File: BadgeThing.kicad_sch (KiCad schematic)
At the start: 63 parts, among them J1 USB_C_Receptacle_USB2.0, J2 Connector_Generic_Conn_01x02, J3 Ext 5V, J4 SWD Header, J6 External 3V3, SW1 BOOTSEL, SW2 ESP RESET, SW3 Left, SW4 Down, SW5 Select, SW6 Up, SW7 Right, U2 W25Q32JVSS, U3 RP2040, U4 NCP1117-3.3_SOT223, U5 ESP-12F, Y1 12.000MHz

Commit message: Continue routing
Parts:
- added C24: 100nF, Capacitor_SMD:C_0402_1005Metric_Pad0.74x0.62mm_HandSolder, symbol Device:C_Small
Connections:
- net +3V3: now also C24.1
- net GND: now also C24.2
- net ESP_RST: now reaches SW2.2, U5.1 (~{RST})
- net ESP13: now reaches U5.7 (GPIO13)
- no-connect marks 38 -> 37
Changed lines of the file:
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@@
   (junction (at 254.635 110.49) (diameter 0) (color 0 0 0 0)
   )
+  (junction (at 213.36 24.13) (diameter 0) (color 0 0 0 0)
+  )
   (junction (at 130.81 35.56) (diameter 0) (color 0 0 0 0)
   )
@@
   (junction (at 128.27 35.56) (diameter 0) (color 0 0 0 0)
   )
+  (junction (at 203.2 19.05) (diameter 0) (color 0 0 0 0)
+  )
   (junction (at 66.675 107.95) (diameter 0) (color 0 0 0 0)
   )
@@
   (no_connect (at 153.67 134.62))
   (no_connect (at 25.4 131.445))
-  (no_connect (at 55.88 131.445))
   (no_connect (at 55.88 126.365))
   (no_connect (at 255.27 137.16))
@@
     (stroke (width 0) (type default))
   )
+  (wire (pts (xy 203.2 24.13) (xy 213.36 24.13))
+    (stroke (width 0) (type default))
+  )
   (polyline (pts (xy 241.935 13.335) (xy 283.845 13.335))
     (stroke (width 0) (type default))
@@
     (stroke (width 0) (type default))
   )
+  (wire (pts (xy 203.2 19.05) (xy 213.36 19.05))
+    (stroke (width 0) (type default))
+  )
   (wire (pts (xy 209.55 137.16) (xy 217.17 137.16))
     (stroke (width 0) (type default))
@@
     (stroke (width 0) (type default))
   )
-  (wire (pts (xy 203.2 24.13) (xy 203.2 24.765))
+  (wire (pts (xy 213.36 24.13) (xy 213.36 24.765))
     (stroke (width 0) (type default))
   )
@@
     (stroke (width 0) (type default))
   )
-  (polyline (pts (xy 165.1 150.495) (xy 263.525 150.495))
+  (polyline (pts (xy 166.37 150.495) (xy 263.525 150.495))
     (stroke (width 0) (type default))
   )
@@
     (stroke (width 0) (type default))
   )
-  (polyline (pts (xy 165.1 119.38) (xy 284.988 119.38))
+  (polyline (pts (xy 166.37 119.38) (xy 284.988 119.38))
     (stroke (width 0) (type default))
   )
@@
     (stroke (width 0) (type default))
   )
-  (polyline (pts (xy 165.1 150.495) (xy 165.1 119.38))
+  (polyline (pts (xy 166.37 150.495) (xy 166.37 119.38))
     (stroke (width 0) (type default))
   )
@@
     (stroke (width 0) (type default))
   )
-  (polyline (pts (xy 76.835 150.495) (xy 165.1 150.495))
+  (polyline (pts (xy 76.835 150.495) (xy 166.37 150.495))
     (stroke (width 0) (type default))
   )
@@
     (effects (font (size 1.27 1.27)) (justify left bottom))
   )
-  (text "RGB LEDs" (at 165.735 121.92 0)
+  (text "RGB LEDs" (at 167.005 121.92 0)
     (effects (font (size 1.27 1.27)) (justify left bottom))
   )
@@
     (effects (font (size 1.27 1.27)) (justify left bottom))
   )
+  (label "ESP_RST" (at 17.145 113.665 0) (fields_autoplaced)
+    (effects (font (size 1.27 1.27)) (justify left bottom))
+  )
   (global_label "SCLK" (shape input) (at 153.67 93.98 0) (fields_autoplaced)
     (effects (font (size 1.27 1.27)) (justify left))
@@
     )
   )
+  (global_label "ESP13" (shape input) (at 55.88 131.445 0) (fields_autoplaced)
+    (effects (font (size 1.27 1.27)) (justify left))
+    (property "Intersheetrefs" "${INTERSHEET_REFS}" (at 64.8333 131.445 0)
+      (effects (font (size 1.27 1.27)) (justify left) hide)
+    )
+  )
   (global_label "ESP0" (shape input) (at 74.93 130.175 270) (fields_autoplaced)
     (effects (font (size 1.27 1.27)) (justify right))
@@
     )
   )
-  (symbol (lib_id "power:GND") (at 203.2 24.765 0) (unit 1)
+  (symbol (lib_id "power:GND") (at 213.36 24.765 0) (unit 1)
     (in_bom yes) (on_board yes) (dnp no) (fields_autoplaced)
-    (property "Reference" "#PWR028" (at 203.2 31.115 0)
+    (property "Reference" "#PWR028" (at 213.36 31.115 0)
       (effects (font (size 1.27 1.27)) hide)
     )
-    (property "Value" "GND" (at 203.2 29.845 0)
+    (property "Value" "GND" (at 213.36 29.845 0)
       (effects (font (size 1.27 1.27)))
     )
-    (property "Footprint" "" (at 203.2 24.765 0)
+    (property "Footprint" "" (at 213.36 24.765 0)
       (effects (font (size 1.27 1.27)) hide)
     )
-    (property "Datasheet" "" (at 203.2 24.765 0)
+    (property "Datasheet" "" (at 213.36 24.765 0)
       (effects (font (size 1.27 1.27)) hide)
     )
@@
   )
   (symbol (lib_id "Device:C_Small") (at 203.2 21.59 0) (unit 1)
-    (in_bom yes) (on_board yes) (dnp no) (fields_autoplaced)
-    (property "Reference" "C22" (at 205.74 20.3262 0)
+    (in_bom yes) (on_board yes) (dnp no)
+    (property "Reference" "C22" (at 205.105 20.32 0)
       (effects (font (size 1.27 1.27)) (justify left))
     )
-    (property "Value" "100nF" (at 205.74 22.8662 0)
+    (property "Value" "100nF" (at 205.105 22.86 0)
       (effects (font (size 1.27 1.27)) (justify left))
     )
@@
         )
       )
+    )
+  )
+  (symbol (lib_id "Device:C_Small") (at 213.36 21.59 0) (unit 1)
+    (in_bom yes) (on_board yes) (dnp no)
+    (property "Reference" "C24" (at 215.265 20.32 0)
+      (effects (font (size 1.27 1.27)) (justify left))
+    )
+    (property "Value" "100nF" (at 215.265 22.86 0)
+      (effects (font (size 1.27 1.27)) (justify left))
+    )
+    (property "Footprint" "Capacitor_SMD:C_0402_1005Metric_Pad0.74x0.62mm_HandSolder" (at 213.36 21.59 0)
+      (effects (font (size 1.27 1.27)) hide)
+    )
+    (property "Datasheet" "~" (at 213.36 21.59 0)
+      (effects (font (size 1.27 1.27)) hide)
+    )
+    (property "LCSC" "C1525" (at 213.36 21.59 0)
+      (effects (font (size 1.27 1.27)) hide)
+    )
+    (pin "1")
+    (pin "2")
+    (instances
+      (project "BadgeThing"
+        (path "/35d5f6bf-e39e-48ab-813a-17587fce37db"
+          (reference "C24") (unit 1)
+        )
+      )
+      (project "PicoLX"
+        (path "/c5e5d8b8-bebd-4318-85a6-adbafb95dd10"
+          (reference "C14") (unit 1)
+        )
+      )
+      (project "Panel"
+        (path "/f55927e3-6490-4e79-9229-dceeb24f0064"
+          (reference "C15") (unit 1)
+        )
+      )

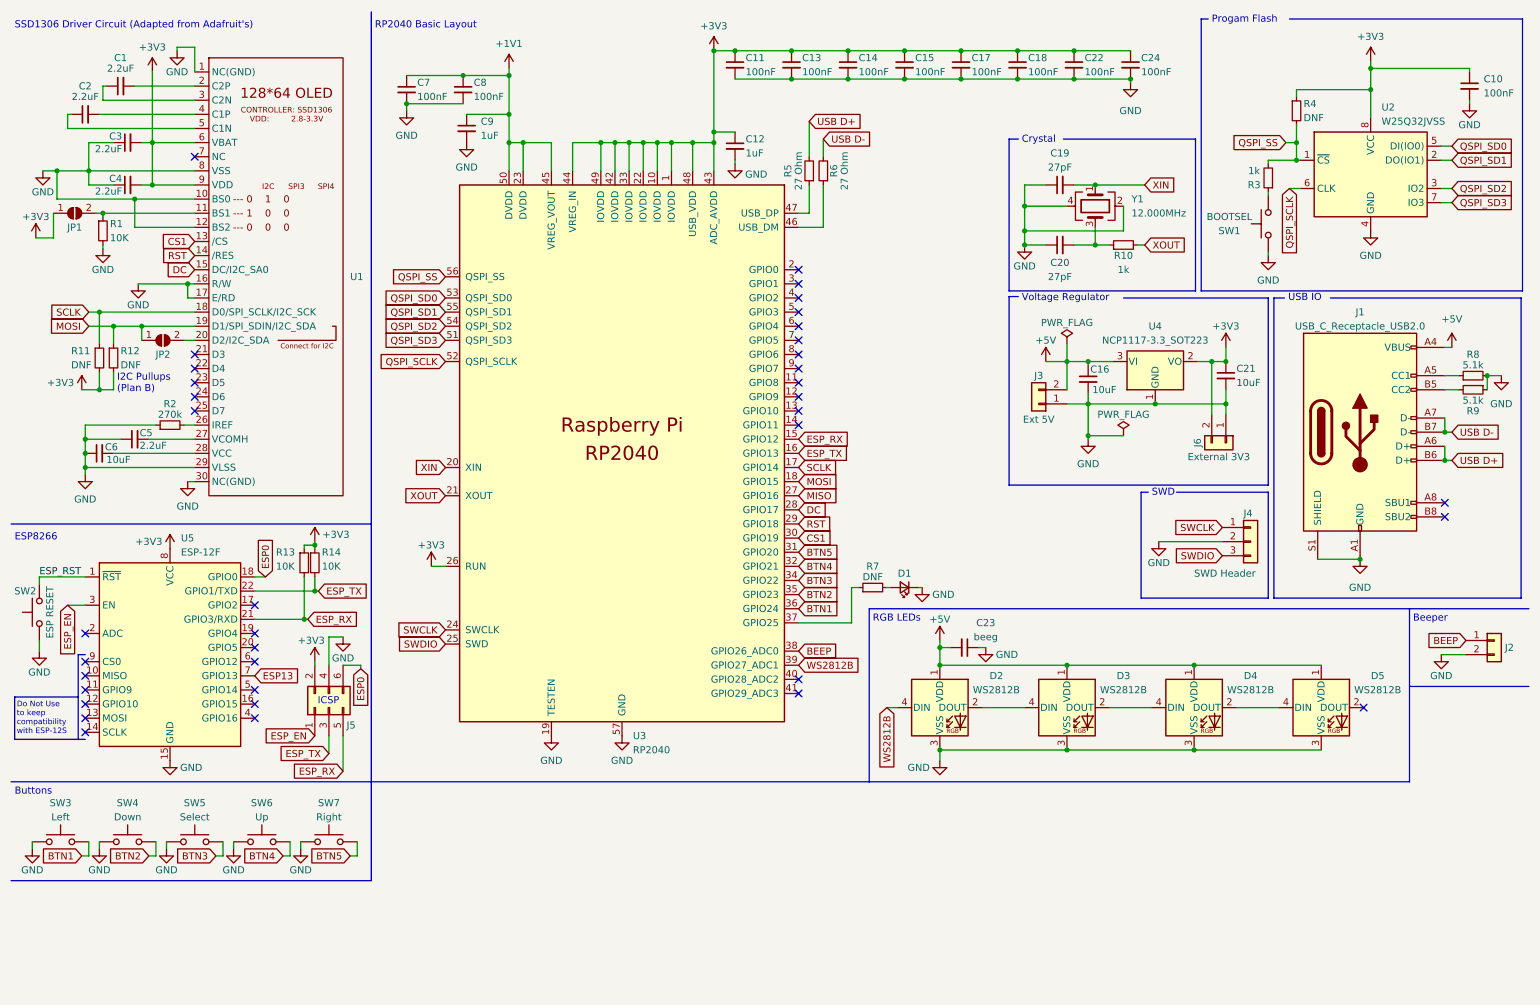
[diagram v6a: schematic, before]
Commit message: huge routing optimizations and extra features
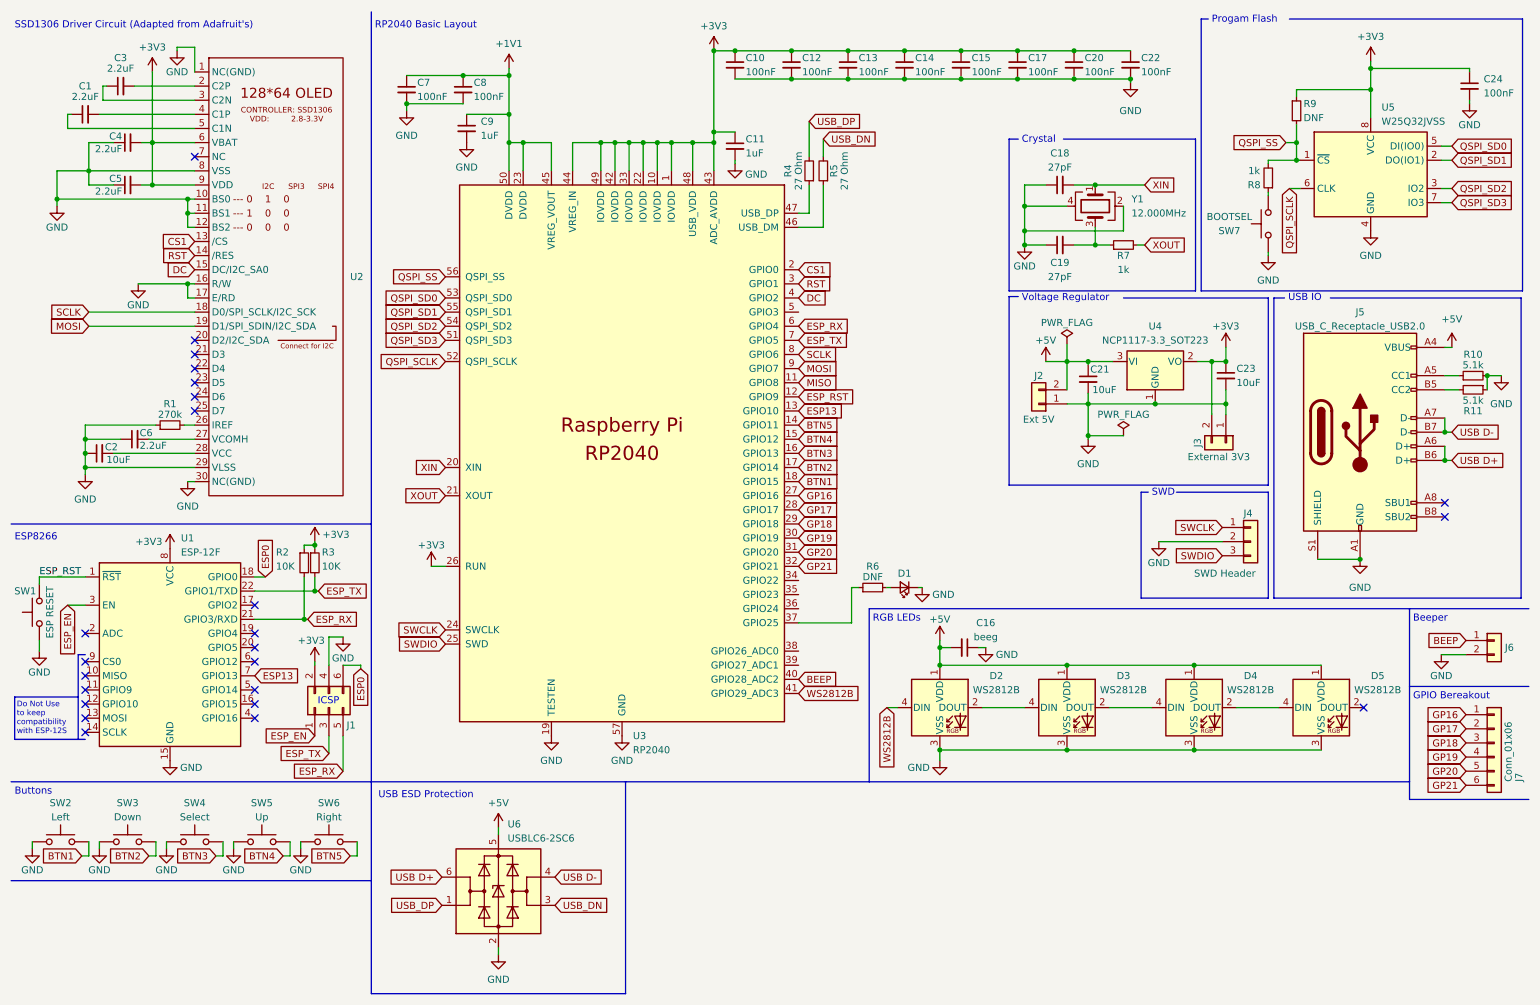
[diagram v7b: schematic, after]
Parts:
- removed JP1, JP2: SolderJumper_2_Open, Jumper:SolderJumper-2_P1.3mm_Open_RoundedPad1.0x1.5mm, symbol Jumper:SolderJumper_2_Open
- removed R1: 10K, Resistor_SMD:R_0402_1005Metric_Pad0.72x0.64mm_HandSolder, symbol Device:R_Small
- removed R11, R12: DNF, Resistor_SMD:R_0402_1005Metric_Pad0.72x0.64mm_HandSolder, symbol Device:R_Small
- added J7: Conn_01x06, Connector_PinHeader_2.00mm:PinHeader_1x06_P2.00mm_Vertical, symbol Connector_Generic:Conn_01x06
- added U6: USBLC6-2SC6, Package_TO_SOT_SMD:SOT-23-6, symbol Power_Protection:USBLC6-2SC6
- C1: renamed from C2; LCSC (none) -> C12530
- C3: renamed from C1; LCSC (none) -> C12530
- C4: renamed from C3; LCSC (none) -> C12530
- C5: renamed from C4; LCSC (none) -> C12530
- C6: renamed from C5; LCSC (none) -> C12530
- renumbered C11 to C10, C12 to C11, C13 to C12, C14 to C13, C15 to C14, C17 to C15, C23 to C16, C18 to C17, C19 to C18, C20 to C19, C6 to C2, C22 to C20, C16 to C21, C24 to C22, C21 to C23, C10 to C24, J5 to J1, J3 to J2, J6 to J3, J1 to J5, J2 to J6, R2 to R1, R8 to R10, R9 to R11, R13 to R2, R14 to R3, R5 to R4, R6 to R5, R7 to R6, R10 to R7, R3 to R8, R4 to R9, SW2 to SW1, SW3 to SW2, SW4 to SW3, SW5 to SW4, SW6 to SW5, SW7 to SW6, SW1 to SW7, U5 to U1, U1 to U2, U2 to U5
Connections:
- net +5V: now also U6.5 (VBUS)
- net BEEP: now also U3.40 (GPIO28_ADC2); no longer U3.38 (GPIO26_ADC0)
- net BTN1: now also U3.18 (GPIO15); no longer U3.36 (GPIO24)
- net BTN2: now also U3.17 (GPIO14); no longer U3.35 (GPIO23)
- net BTN3: now also U3.16 (GPIO13); no longer U3.34 (GPIO22)
- net BTN4: now also U3.15 (GPIO12); no longer U3.32 (GPIO21)
- net BTN5: now also U3.14 (GPIO11); no longer U3.31 (GPIO20)
- net CS1: now also U3.2 (GPIO0); no longer U3.30 (GPIO19)
- net DC: now also U3.4 (GPIO2); no longer U3.28 (GPIO17)
- net ESP13: now also U3.13 (GPIO10)
- net ESP_RST: now also U3.12 (GPIO9)
- net ESP_RX: now also U3.6 (GPIO4); no longer U3.15 (GPIO12)
- net ESP_TX: now also U3.7 (GPIO5); no longer U3.16 (GPIO13)
- net GND: now also U2.11 (BS1), U6.2 (GND)
- net MISO: now also U3.11 (GPIO8); no longer U3.27 (GPIO16)
- net MOSI: now also U3.9 (GPIO7); no longer U3.18 (GPIO15)
- net RST: now also U3.3 (GPIO1); no longer U3.29 (GPIO18)
- net SCLK: now also U3.8 (GPIO6); no longer U3.17 (GPIO14)
- net USB D+: now also U6.6 (I/O1); no longer R4.2
- net USB D-: now also U6.4 (I/O2); no longer R5.2
- net WS2812B: now also U3.41 (GPIO29_ADC3); no longer U3.39 (GPIO27_ADC1)
- new net GP16: J7.1 (Pin_1), U3.27 (GPIO16)
- new net GP17: J7.2 (Pin_2), U3.28 (GPIO17)
- new net GP18: J7.3 (Pin_3), U3.29 (GPIO18)
- new net GP19: J7.4 (Pin_4), U3.30 (GPIO19)
- new net GP20: J7.5 (Pin_5), U3.31 (GPIO20)
- new net GP21: J7.6 (Pin_6), U3.32 (GPIO21)
- new net USB_DN: R5.2, U6.3 (I/O2)
- new net USB_DP: R4.2, U6.1 (I/O1)
- no-connect marks 37 -> 24
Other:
- note added: "GPIO Bereakout"
- note added: "USB ESD Protection"
- note removed: "I2C Pullups (Plan B)"

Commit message: Final routing
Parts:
- added R12: 4.7k, Resistor_SMD:R_0402_1005Metric_Pad0.72x0.64mm_HandSolder, symbol Device:R_Small
- U6: LCSC C111212 -> C2687116
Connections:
- net ESP0: now also U3.34 (GPIO22)
- net GND: now also R12.1
- net RST: now also R12.2
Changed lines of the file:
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@@
   (junction (at 25.4 88.9) (diameter 0) (color 0 0 0 0)
   )
+  (junction (at 33.02 45.72) (diameter 0) (color 0 0 0 0)
+  )
   (junction (at 201.93 74.93) (diameter 0) (color 0 0 0 0)
   )
@@
   (junction (at 179.07 126.365) (diameter 0) (color 0 0 0 0)
   )
+  (junction (at 33.02 55.88) (diameter 0) (color 0 0 0 0)
+  )
   (junction (at 243.205 38.735) (diameter 0) (color 0 0 0 0)
   )
@@
     (stroke (width 0) (type default))
   )
+  (wire (pts (xy 31.115 55.88) (xy 33.02 55.88))
+    (stroke (width 0) (type default))
+  )
   (wire (pts (xy 162.56 19.05) (xy 172.72 19.05))
     (stroke (width 0) (type default))
@@
     (stroke (width 0) (type default))
   )
+  (wire (pts (xy 33.02 45.72) (xy 33.02 48.26))
+    (stroke (width 0) (type default))
+  )
   (wire (pts (xy 238.125 55.88) (xy 238.125 55.245))
     (stroke (width 0) (type default))
@@
     (stroke (width 0) (type default))
   )
+  (wire (pts (xy 33.02 45.72) (xy 43.815 45.72))
+    (stroke (width 0) (type default))
+  )
   (polyline (pts (xy 191.516 34.925) (xy 193.167 34.925))
     (stroke (width 0) (type default))
@@
     (stroke (width 0) (type default))
   )
+  (wire (pts (xy 33.02 55.88) (xy 45.085 55.88))
+    (stroke (width 0) (type default))
+  )
   (wire (pts (xy 227.965 74.93) (xy 227.965 84.455))
     (stroke (width 0) (type default))
@@
     (stroke (width 0) (type default))
   )
-  (wire (pts (xy 20.32 45.72) (xy 43.815 45.72))
-    (stroke (width 0) (type default))
-  )
   (wire (pts (xy 43.815 60.96) (xy 43.815 63.5))
     (stroke (width 0) (type default))
@@
     (stroke (width 0) (type default))
   )
+  (wire (pts (xy 33.02 53.34) (xy 33.02 55.88))
+    (stroke (width 0) (type default))
+  )
   (polyline (pts (xy 263.525 153.67) (xy 284.988 153.67))
     (stroke (width 0) (type default))
@@
     (stroke (width 0) (type default))
   )
+  (wire (pts (xy 20.32 45.72) (xy 33.02 45.72))
+    (stroke (width 0) (type default))
+  )
   (wire (pts (xy 74.295 163.83) (xy 73.025 163.83))
     (stroke (width 0) (type default))
@@
     )
   )
+  (global_label "ESP0" (shape input) (at 153.67 114.3 0) (fields_autoplaced)
+    (effects (font (size 1.27 1.27)) (justify left))
+    (property "Intersheetrefs" "${INTERSHEET_REFS}" (at 161.4138 114.3 0)
+      (effects (font (size 1.27 1.27)) (justify left) hide)
+    )
+  )
   (global_label "ESP13" (shape input) (at 153.67 83.82 0) (fields_autoplaced)
     (effects (font (size 1.27 1.27)) (justify left))
@@
     )
   )
-  (global_label "RST" (shape input) (at 45.085 55.88 180) (fields_autoplaced)
+  (global_label "RST" (shape input) (at 31.115 55.88 180) (fields_autoplaced)
     (effects (font (size 1.27 1.27)) (justify right))
-    (property "Intersheetrefs" "${INTERSHEET_REFS}" (at 38.7321 55.88 0)
+    (property "Intersheetrefs" "${INTERSHEET_REFS}" (at 24.7621 55.88 0)
       (effects (font (size 1.27 1.27)) (justify right) hide)
     )
@@
       (effects (font (size 1.27 1.27)) hide)
     )
-    (property "LCSC" "C111212" (at 99.695 170.18 0)
+    (property "LCSC" "C2687116" (at 99.695 170.18 0)
       (effects (font (size 1.27 1.27)) hide)
     )
@@
         )
       )
+    )
+  )
+  (symbol (lib_id "Device:R_Small") (at 33.02 50.8 0) (unit 1)
+    (in_bom yes) (on_board yes) (dnp no)
+    (property "Reference" "R12" (at 34.29 49.53 0)
+      (effects (font (size 1.27 1.27)) (justify left))
+    )
+    (property "Value" "4.7k" (at 34.29 52.07 0)
+      (effects (font (size 1.27 1.27)) (justify left))
+    )
+    (property "Footprint" "Resistor_SMD:R_0402_1005Metric_Pad0.72x0.64mm_HandSolder" (at 33.02 50.8 0)
+      (effects (font (size 1.27 1.27)) hide)
+    )
+    (property "Datasheet" "~" (at 33.02 50.8 0)
+      (effects (font (size 1.27 1.27)) hide)
+    )
+    (property "LCSC" "C25900" (at 33.02 50.8 0)
+      (effects (font (size 1.27 1.27)) hide)
+    )
+    (pin "1")
+    (pin "2")
+    (instances
+      (project "BadgeThing"
+        (path "/35d5f6bf-e39e-48ab-813a-17587fce37db"
+          (reference "R12") (unit 1)
+        )
+      )
